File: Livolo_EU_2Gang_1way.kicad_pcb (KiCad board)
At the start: 2 copper layers, 43 x 43 mm, 39 parts, among them IC1 ATMEGA328P, U1 ATSHA204A, U2 RFM69_MINIMAL

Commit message: cleanup schema
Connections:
- net /N$1 renamed Net-(D6-Pad2)
- net /N$10 renamed Net-(D4-Pad1)
- net /N$14 renamed Net-(U$7-PadP$1)
- net /N$2 renamed Net-(IC1-Pad7)
- net /N$3 renamed Net-(C4-Pad2)
- net /N$4 renamed Net-(C2-Pad2)
- net /N$5 renamed Net-(D1-Pad2)
- net /N$6 renamed Net-(D2-Pad1)
- net /N$7 renamed Net-(D3-Pad2)
- net /N$8 renamed Net-(IC1-Pad8)
- net /N$9 renamed Net-(C8-Pad2)

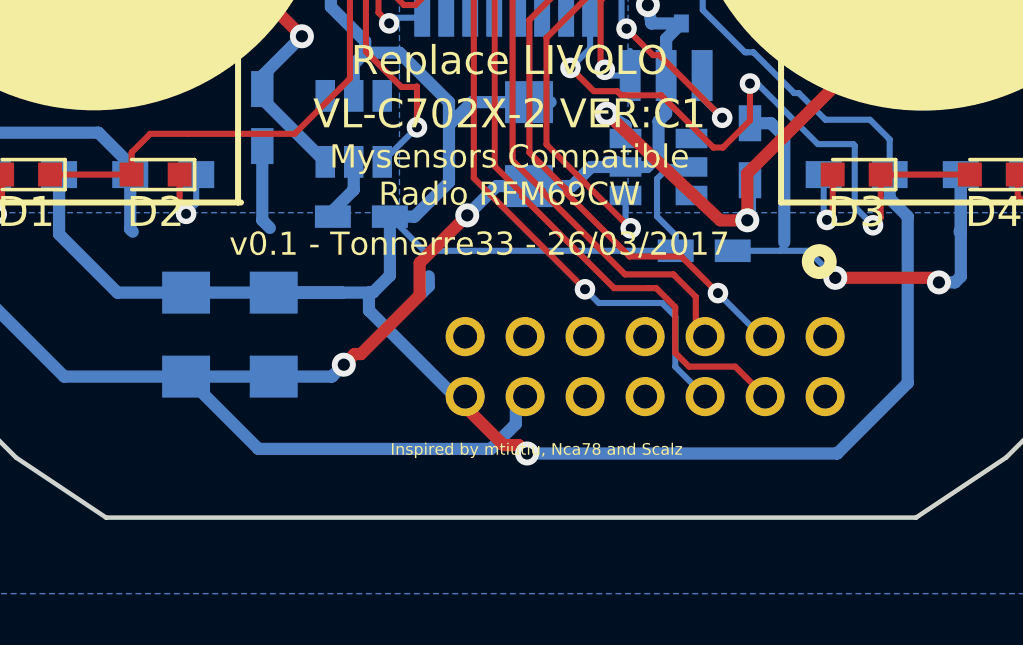
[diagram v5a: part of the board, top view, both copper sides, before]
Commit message: Ceramic capacitor added in parrallel of Tantalum
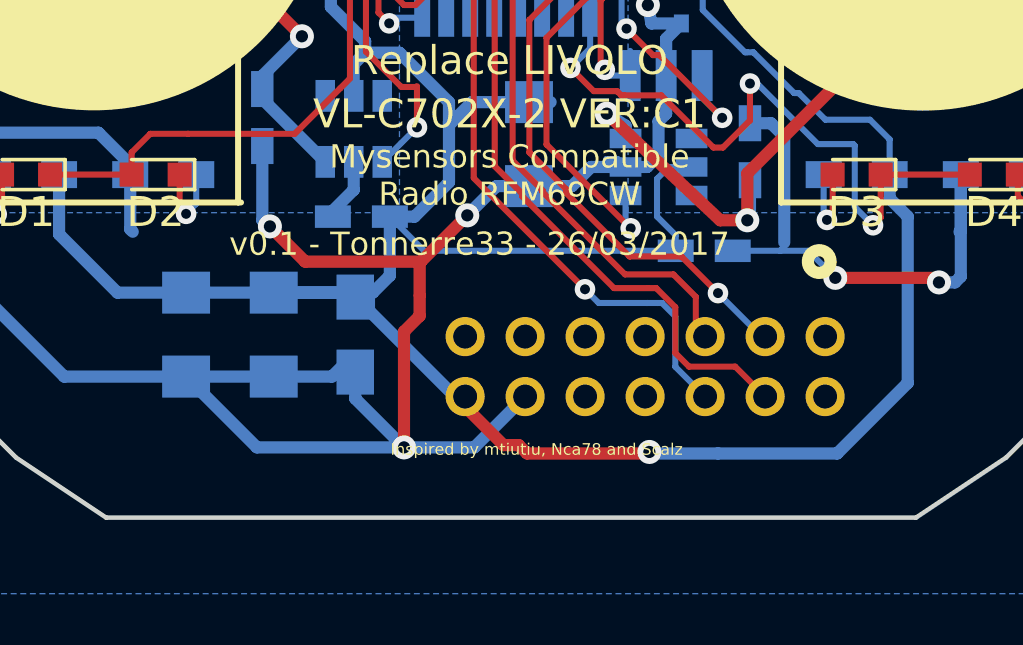
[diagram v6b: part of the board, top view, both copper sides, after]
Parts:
- added C13: 100n, Capacitors_SMD:C_0805_HandSoldering, B.Cu at (143.3, 120.4)
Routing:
- net GND: track 170.4 -> 180.7 mm, vias 14 -> 15
- net (no net): track 5.86 -> 5.10 mm

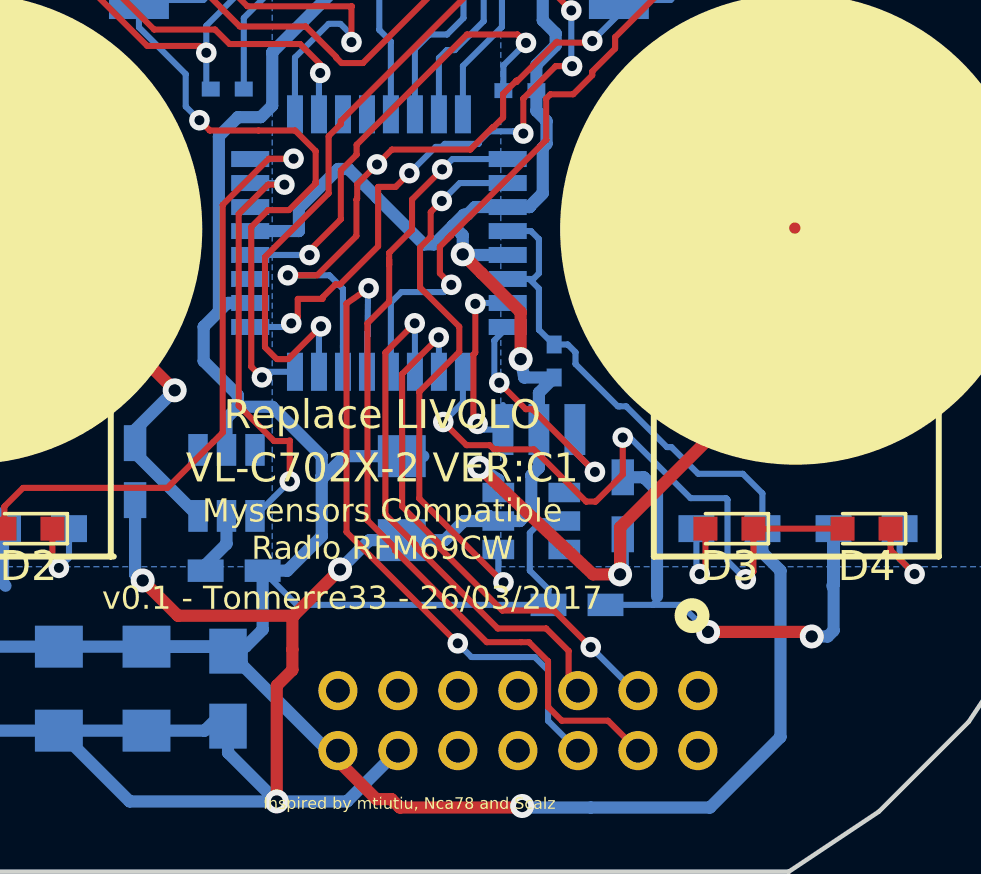
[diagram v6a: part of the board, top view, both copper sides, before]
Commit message: optimise position condensator senspad
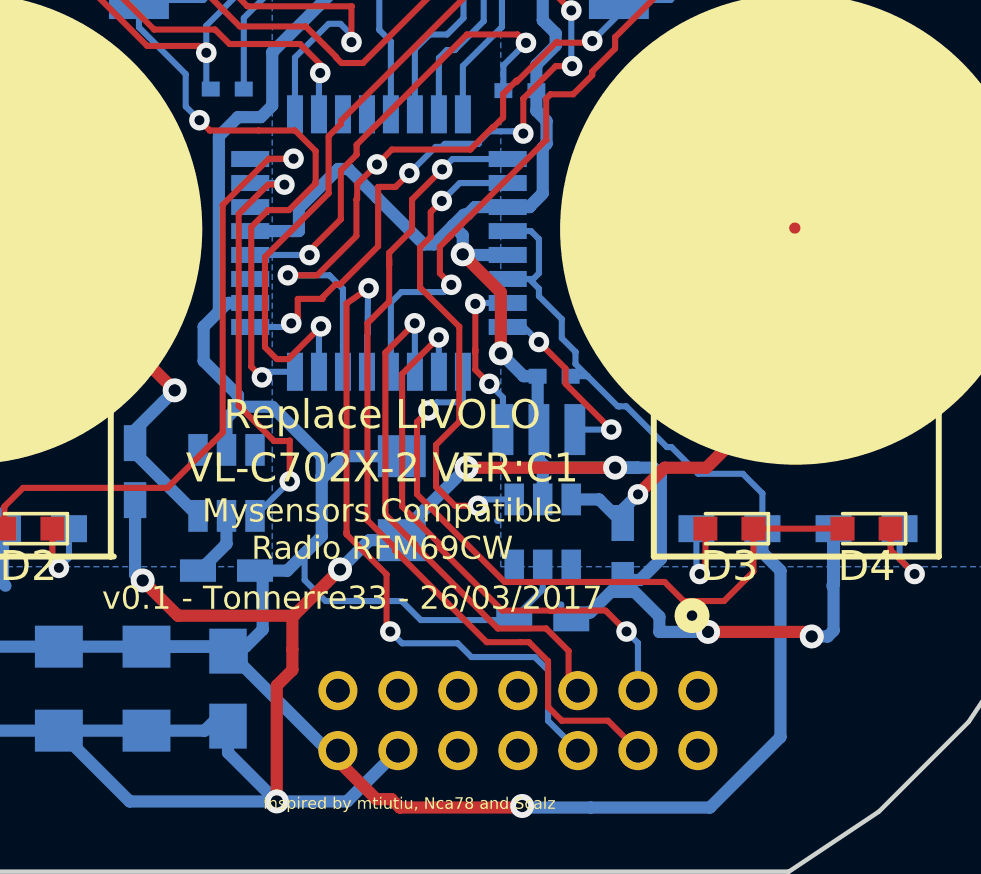
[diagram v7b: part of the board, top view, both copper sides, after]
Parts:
- moved C4 1.52 mm to (156.5, 115.8), turned to 90 degrees
- moved C7 1.25 mm to (153.8, 118.1)
- moved U$4 0.54 mm to (153.8, 115.2), turned to 270 degrees
- moved C6 0.51 mm to (154.2, 110.0), turned to 0 degrees
- moved C9 0.26 mm to (143.3, 116.5)
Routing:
- net GND: track 180.7 -> 188.0 mm, vias 15 -> 17
- net VCC: track 177.5 -> 173.6 mm
- net Net-(C4-Pad2): track 22.6 -> 19.3 mm, vias 2 -> 1
- net /TOUCH_1: track 18.9 -> 16.1 mm
- net Net-(IC1-Pad8): track 8.22 -> 6.38 mm
- net /L2_SET: track 17.6 -> 19.1 mm
- net /L1_SET: track 23.0 -> 24.1 mm
- net /LED2: track 22.8 -> 22.7 mm, vias 3 -> 1
